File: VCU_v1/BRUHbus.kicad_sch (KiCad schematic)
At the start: 26 parts, among them J5 BRUHBus, J6 BRUHBus, J7 BRUHBus, J8 BRUHBus, Q2 BSD235NH6327XT, Q6 BSD235NH6327XT

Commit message: begin pcb design
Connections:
- net +24V: now also J7.4 (+Vs), J8.4 (+Vs); no longer J7.6 (+Vs), J8.6 (+Vs)
- net CAN1_H: now also J5.1 (CANH_OUT), J7.1 (CANH_OUT); no longer J5.2 (CANH_OUT), J7.2 (CANH_OUT)
- net CAN1_L: now also J5.2 (CANL_OUT), J7.2 (CANL_OUT); no longer J5.1 (CANL_OUT), J7.1 (CANL_OUT)
- net CAN2_H: now also J6.1 (CANH_OUT), J8.1 (CANH_OUT); no longer J6.2 (CANH_OUT), J8.2 (CANH_OUT)
- net CAN2_L: now also J6.2 (CANL_OUT), J8.2 (CANL_OUT); no longer J6.1 (CANL_OUT), J8.1 (CANL_OUT)
- net GND: now also J5.6 (-Vs), J6.6 (-Vs), J7.6 (-Vs), J8.6 (-Vs); no longer J5.4 (-Vs), J6.4 (-Vs), J7.4 (-Vs), J8.4 (-Vs)
- net Vin: now also J5.4 (+Vs), J6.4 (+Vs); no longer J5.6 (+Vs), J6.6 (+Vs)

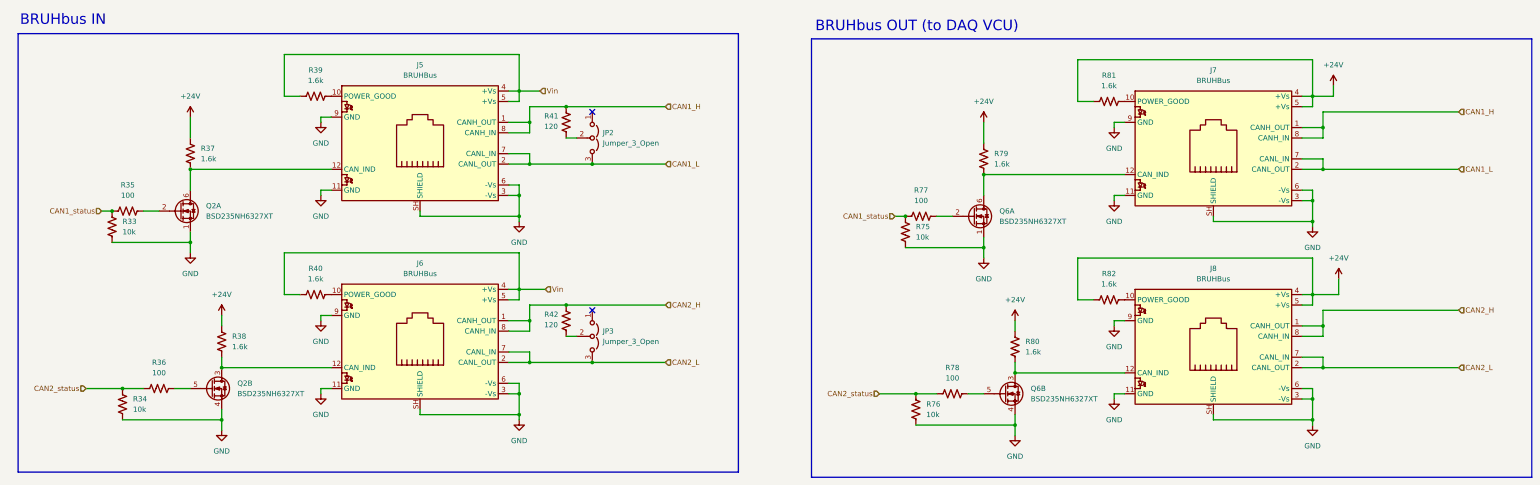
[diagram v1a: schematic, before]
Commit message: vcu placements complete
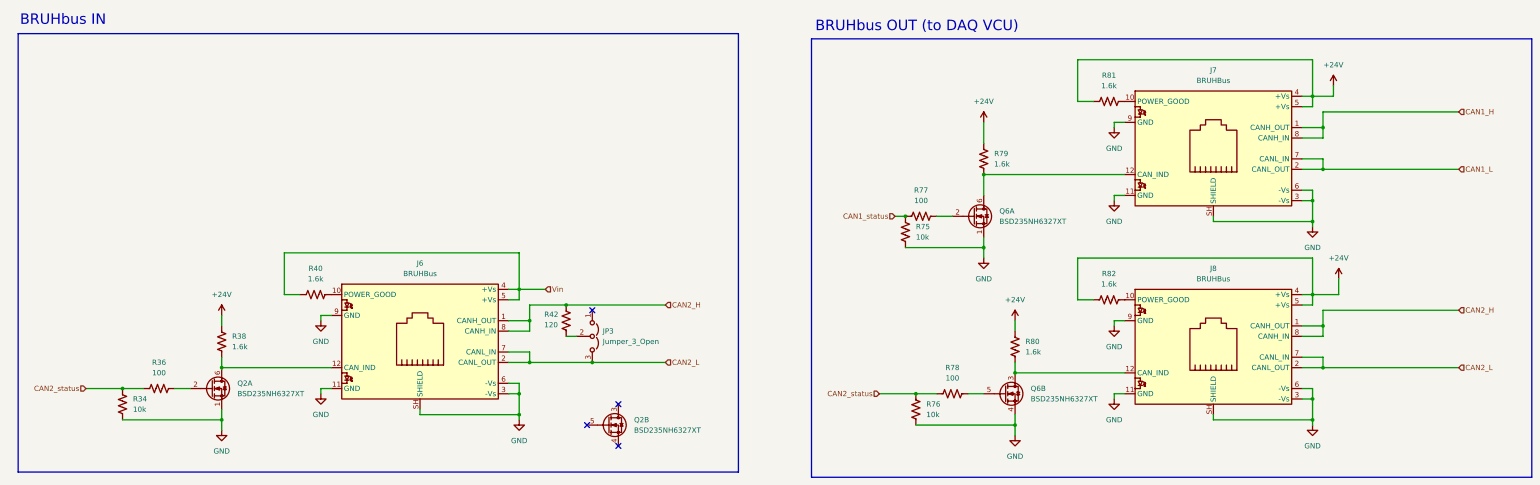
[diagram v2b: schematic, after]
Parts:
- removed J5: BRUHBus, Connector_RJ:RJ45_Amphenol_RJHSE538X, symbol BFR Connectors:BRUHbus
- removed JP2: Jumper_3_Open, Connector_PinHeader_2.54mm:PinHeader_1x03_P2.54mm_Vertical, symbol Jumper:Jumper_3_Open
- removed R33: 10k, Resistor_SMD:R_0603_1608Metric_Pad0.98x0.95mm_HandSolder, symbol BFR Resistors:RMCF0603FT10K0
- removed R35: 100, Resistor_SMD:R_0603_1608Metric_Pad0.98x0.95mm_HandSolder, symbol BFR Resistors:RMCF0603FT100R
- removed R37, R39: 1.6k, Resistor_SMD:R_0603_1608Metric_Pad0.98x0.95mm_HandSolder, symbol BFR Resistors:RMCF0603FT1K60
- removed R41: 120, Resistor_SMD:R_0603_1608Metric_Pad0.98x0.95mm_HandSolder, symbol BFR Resistors:RMCF0603FT120R
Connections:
- net GND: no longer Q2.4 (S)
- net at J6.12 (CAN_IND), R38.1: now also Q2.6 (D); no longer Q2.3 (D)
- net at R36.2: now also Q2.2 (G); no longer Q2.5 (G)
- no-connect marks 2 -> 4

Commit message: stm power routing complete, power polygons done
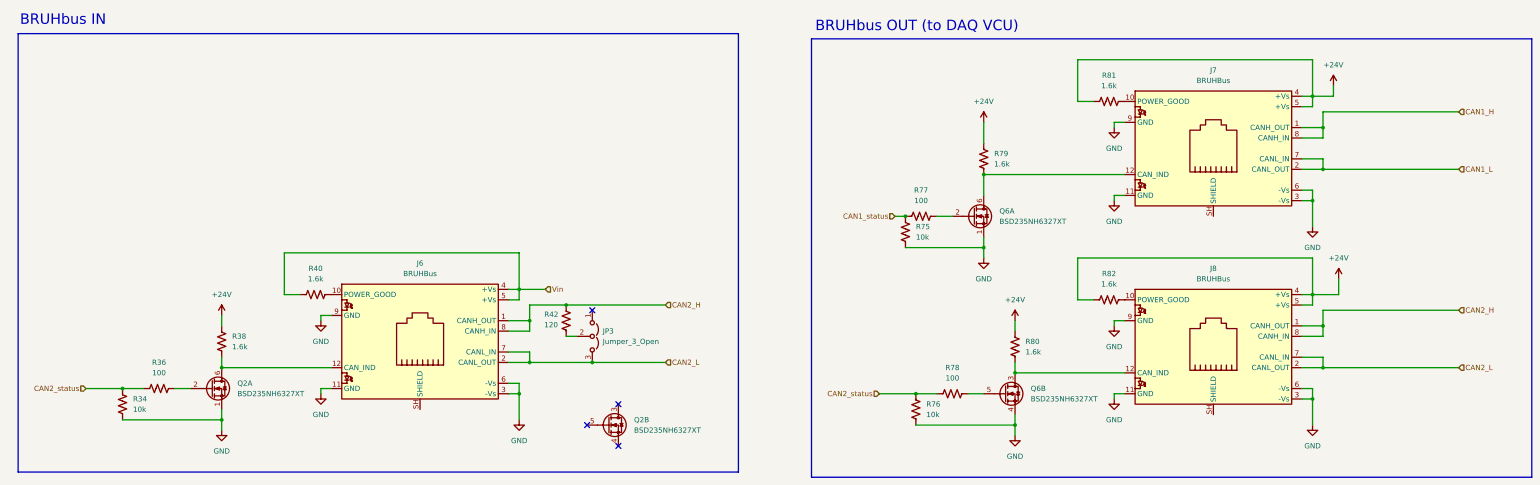
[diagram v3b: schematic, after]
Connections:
- net GND: no longer J6.SH (SHIELD), J7.SH (SHIELD), J8.SH (SHIELD)
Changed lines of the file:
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@@
-	)
-	(junction
-		(at 330.2 113.03)
-		(diameter 0)
-		(color 0 0 0 0)
 	)
 	(junction
@@
 	)
 	(junction
-		(at 330.2 64.77)
-		(diameter 0)
-		(color 0 0 0 0)
-	)
-	(junction
 		(at 154.94 99.06)
 		(diameter 0)
@@
 	(junction
 		(at 330.2 82.55)
-		(diameter 0)
-		(color 0 0 0 0)
-	)
-	(junction
-		(at 137.16 111.76)
 		(diameter 0)
 		(color 0 0 0 0)
@@
 	(wire
 		(pts
-			(xy 306.07 64.77) (xy 330.2 64.77)
-		)
-		(stroke
-			(width 0)
-			(type default)
-		)
-	)
-	(wire
-		(pts
 			(xy 88.9 105.41) (xy 88.9 106.68)
 		)
@@
 	(wire
 		(pts
-			(xy 113.03 110.49) (xy 113.03 111.76)
-		)
-		(stroke
-			(width 0)
-			(type default)
-		)
-	)
-	(wire
-		(pts
 			(xy 332.74 86.36) (xy 332.74 90.17)
 		)
@@
 	(wire
 		(pts
-			(xy 306.07 111.76) (xy 306.07 113.03)
-		)
-		(stroke
-			(width 0)
-			(type default)
-		)
-	)
-	(wire
-		(pts
 			(xy 332.74 90.17) (xy 327.66 90.17)
 		)
@@
 	(wire
 		(pts
-			(xy 330.2 107.95) (xy 330.2 113.03)
-		)
-		(stroke
-			(width 0)
-			(type default)
-		)
-	)
-	(wire
-		(pts
 			(xy 137.16 83.82) (xy 137.16 81.28)
 		)
@@
 	(wire
 		(pts
-			(xy 306.07 63.5) (xy 306.07 64.77)
-		)
-		(stroke
-			(width 0)
-			(type default)
-		)
-	)
-	(wire
-		(pts
 			(xy 327.66 59.69) (xy 330.2 59.69)
 		)
@@
 	(wire
 		(pts
-			(xy 330.2 64.77) (xy 330.2 66.04)
-		)
-		(stroke
-			(width 0)
-			(type default)
-		)
-	)
-	(wire
-		(pts
-			(xy 330.2 59.69) (xy 330.2 64.77)
+			(xy 330.2 59.69) (xy 330.2 66.04)
 		)
 		(stroke
@@
 	(wire
 		(pts
-			(xy 113.03 111.76) (xy 137.16 111.76)
-		)
-		(stroke
-			(width 0)
-			(type default)
-		)
-	)
-	(wire
-		(pts
 			(xy 139.7 99.06) (xy 154.94 99.06)
 		)
@@
 	(wire
 		(pts
-			(xy 306.07 113.03) (xy 330.2 113.03)
-		)
-		(stroke
-			(width 0)
-			(type default)
-		)
-	)
-	(wire
-		(pts
 			(xy 276.86 35.56) (xy 273.05 35.56)
 		)
@@
 	(wire
 		(pts
-			(xy 330.2 113.03) (xy 330.2 114.3)
+			(xy 330.2 107.95) (xy 330.2 114.3)
 		)
 		(stroke
@@
 	(wire
 		(pts
-			(xy 137.16 111.76) (xy 137.16 113.03)
-		)
-		(stroke
-			(width 0)
-			(type default)
-		)
-	)
-	(wire
-		(pts
 			(xy 233.68 114.3) (xy 257.81 114.3)
 		)
@@
 	(wire
 		(pts
-			(xy 137.16 106.68) (xy 137.16 111.76)
-		)
-		(stroke
+			(xy 137.16 106.68) (xy 137.16 113.03)
+		)
+		(stroke

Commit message: aughhhh
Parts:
- added R33, R35, R37: 0, Resistor_SMD:R_0805_2012Metric_Pad1.20x1.40mm_HandSolder, symbol bfr_resistors:RMCF0805ZT0R00
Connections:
- net GND: now also R33.1, R35.1, R37.1
- net at J6.SH (SHIELD): now also R33.2
- net at J8.SH (SHIELD): now also R37.2
- net at J7.SH (SHIELD): now also R35.2
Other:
- moved on the sheet: J7, Q6A, R75, R77, R79, R81

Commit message: almost done i promise
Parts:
- removed R38, R40, R79, R80, R81, R82: 1.6k, Resistor_SMD:R_0603_1608Metric_Pad0.98x0.95mm_HandSolder, symbol BFR Resistors:RMCF0603FT1K60
- added R12, R17, R18, R21, R38, R39: 2.4k, Resistor_SMD:R_0603_1608Metric_Pad0.98x0.95mm_HandSolder, symbol BFR Resistors:RMCF0603FT2K40
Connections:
- net GND: no longer J6.3 (-Vs), J6.6 (-Vs)
- net at J6.10 (POWER_GOOD): now also R12.2
- net at J6.12 (CAN_IND), Q2.6 (D): now also R17.1
- net at J8.10 (POWER_GOOD): now also R21.2
- net at J7.12 (CAN_IND), Q6.6 (D): now also R38.1
- net at J8.12 (CAN_IND), Q6.3 (D): now also R39.1
- net at J7.10 (POWER_GOOD): now also R18.2
- net +24V renamed +12V
- net +12V: now also R17.2, R18.1, R21.1, R38.2, R39.2
- net Vin: no longer names the net of J6.4 (+Vs), J6.5 (+Vs)
- net Vin: now also R12.1
- no-connect marks 4 -> 6
